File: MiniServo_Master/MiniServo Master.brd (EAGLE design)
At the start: 25.1 x 34.3 mm, 27 parts, among them Q1 16MHz, U1 ATMEGA328, U2 MIC5205

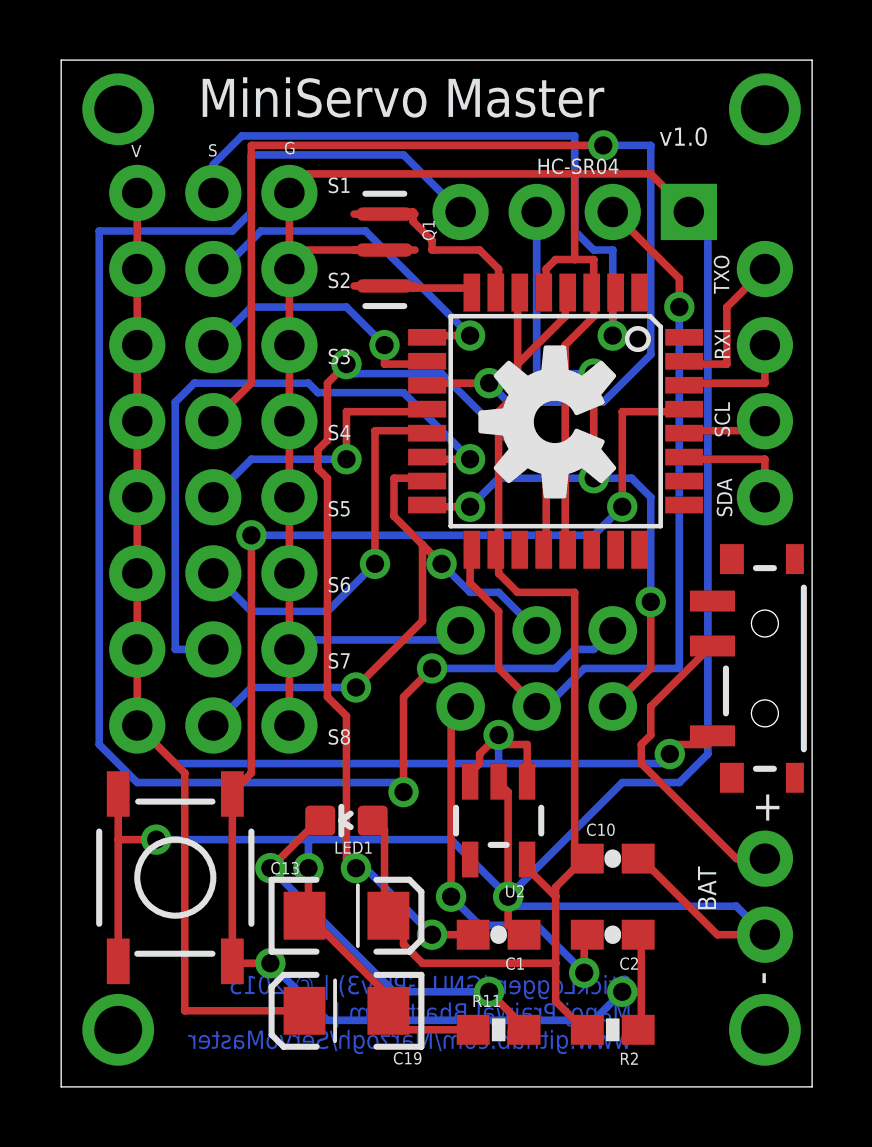
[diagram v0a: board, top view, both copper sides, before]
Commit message: fixed board routing and vias
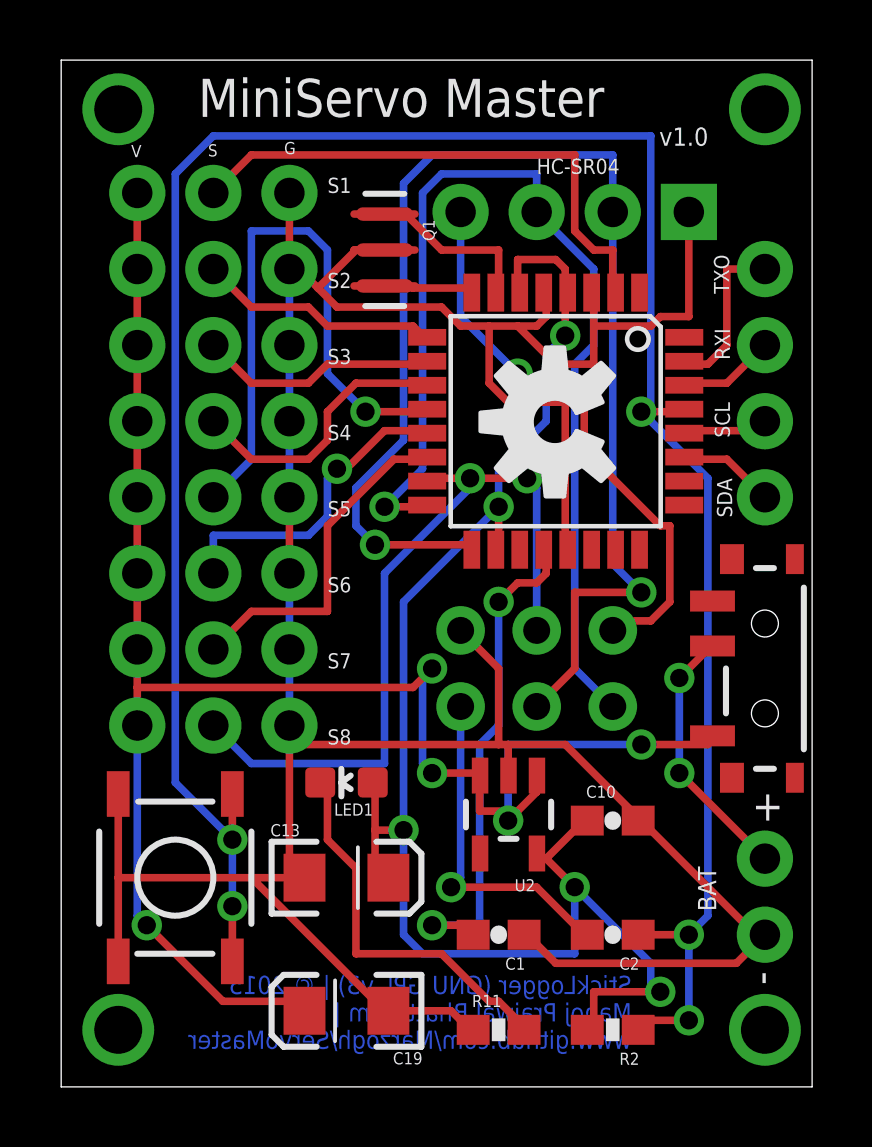
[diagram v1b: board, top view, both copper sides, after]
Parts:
- moved C10 1.27 mm to (18.4, 8.89)
- moved C13 1.27 mm to (9.53, 6.99)
- moved LED1 1.27 mm to (9.53, 10.2)
- moved U2 0.39 mm to (14.9, 9.09)
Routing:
- net 3.3V: track 54.1 -> 19.5 mm, vias 2 -> 1
- net RESET: track 50.8 -> 81.0 mm, vias 4 -> 5
- net D7: track 38.5 -> 9.29 mm, vias 2 -> 0
- net GND: track 133.2 -> 111.3 mm, vias 3 -> 0
- net SCK/ECHO: track 27.6 -> 45.3 mm, vias 1 -> 2
- net AREF: track 33.4 -> 16.9 mm, vias 4 -> 2
- net D8: track 9.27 -> 20.2 mm
- net D10: track 22.1 -> 11.5 mm, vias 1 -> 0
- net VCC: track 43.8 -> 53.8 mm, vias 0 -> 5
- net MISO/TRIG: track 26.4 -> 35.9 mm, vias 4 -> 1
- net MOSI: track 19.7 -> 25.5 mm
- net D4: track 22.4 -> 18.1 mm, vias 1 -> 0
- net D5: track 12.0 -> 8.07 mm, vias 1 -> 0
- net RAW: track 57.6 -> 60.3 mm, vias 2 -> 5
- net D9: track 12.8 -> 10.6 mm
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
